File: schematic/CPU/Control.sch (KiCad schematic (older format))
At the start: 62 parts, among them U44 74LS273, U45 74LS273, U48 28C64, U49 28C64, U61 74LS08, U62 74LS86, U63 74LS374, U64 74LS00, U65 74LS32, U66 74LS08, U67 74LS08, U68 NA555P

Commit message: schematic finished
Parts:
- removed C4: 10nF, symbol Device:C_Small
- removed C5, C6: 0.1uF, symbol Device:C_Small
- removed D33: instrWE, LED_THT:LED_D3.0mm, symbol Device:LED
- removed D34: instrSel, LED_THT:LED_D3.0mm, symbol Device:LED
- removed D35: ~aluOE~, LED_THT:LED_D3.0mm, symbol Device:LED
- removed D36: aluYWE, LED_THT:LED_D3.0mm, symbol Device:LED
- removed D37: reg0WE, LED_THT:LED_D3.0mm, symbol Device:LED
- removed D38: reg1WE, LED_THT:LED_D3.0mm, symbol Device:LED
- removed D39: regBusSel, LED_THT:LED_D3.0mm, symbol Device:LED
- removed D40: ~regBusOE~, LED_THT:LED_D3.0mm, symbol Device:LED
- removed D41: aluSel, LED_THT:LED_D3.0mm, symbol Device:LED
- removed D42: marWE, LED_THT:LED_D3.0mm, symbol Device:LED
- removed D43: ramWE, LED_THT:LED_D3.0mm, symbol Device:LED
- removed D44: ramOE, LED_THT:LED_D3.0mm, symbol Device:LED
- removed D45, D47, D50: LED, LED_THT:LED_D3.0mm, symbol Device:LED
- removed D46: ramSelect, LED_THT:LED_D3.0mm, symbol Device:LED
- removed D48: ~pcOE~, LED_THT:LED_D3.0mm, symbol Device:LED
- removed D49: ~inOE~, LED_THT:LED_D3.0mm, symbol Device:LED
- removed D51: pcIncr, LED_THT:LED_D3.0mm, symbol Device:LED
- removed R33, R34, R35, R36, R37, R38, R39, R40, R41, R42, R43, R44, R45, R46, R47, R48, R49, R50, R51, R54, R58: 1k, Resistor_THT:R_Axial_DIN0207_L6.3mm_D2.5mm_P7.62mm_Horizontal, symbol Device:R
- removed R55: 10k, Resistor_THT:R_Axial_DIN0207_L6.3mm_D2.5mm_P7.62mm_Horizontal, symbol Device:R
- removed U68: NA555P, Package_DIP:DIP-8_W7.62mm, symbol Timer:NA555P
- added D? (x8): LED, LED_THT:LED_D3.0mm, symbol Device:LED
- added R? (x8): 1k, Resistor_THT:R_Axial_DIN0207_L6.3mm_D2.5mm_P7.62mm_Horizontal, symbol Device:R
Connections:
- net labels added: ca0, ca1, ca2, ca3, ca4, ca5, ca6, ca7, halt
- net labels removed: haltPulse
- wire segments 140 -> 114
- no-connect marks 29 -> 28
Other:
- moved on the sheet: R59, R60, R61, U44, U45, U61A, U61B, U61C, U61D, U61E, U62A, U62B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

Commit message: pre upgrade to vivado 2021
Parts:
- gave numbers to parts that had none: 16
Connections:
- net labels added: ~ctrlReg0WE~, ~ctrlReg1WE~
- net labels removed: ctrlReg0WE, ctrlReg1WE
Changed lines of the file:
@@
 $Descr A3 16535 11693
 encoding utf-8
-Sheet 16 19
+Sheet 15 20
 Title ""
 Date ""
@@
 ctrlAluSub
 Text GLabel 8350 5350 2    50   Output ~ 0
-ctrlReg0WE
+~ctrlReg0WE~
 Text GLabel 8350 5450 2    50   Output ~ 0
-ctrlReg1WE
+~ctrlReg1WE~
 Text GLabel 8350 5750 2    50   Output ~ 0
 ctrlAluSel
@@
 AR Path="/601B5CAE/622ED502" Ref="R?"  Part="1"
 AR Path="/6015C763/622ED502" Ref="R?"  Part="1"
-AR Path="/601BB1C4/622ED502" Ref="R?"  Part="1"
-F 0 "R?" V 9443 7750 50  0000 C CNN
+AR Path="/601BB1C4/622ED502" Ref="R43"  Part="1"
+F 0 "R43" V 9443 7750 50  0000 C CNN
 F 1 "1k" V 9534 7750 50  0000 C CNN
 F 2 "Resistor_THT:R_Axial_DIN0207_L6.3mm_D2.5mm_P7.62mm_Horizontal" V 9580 7750 50  0001 C CNN
@@
 AR Path="/601B5CAE/622ED508" Ref="D?"  Part="1"
 AR Path="/6015C763/622ED508" Ref="D?"  Part="1"
-AR Path="/601BB1C4/622ED508" Ref="D?"  Part="1"
-F 0 "D?" H 9993 7495 50  0000 C CNN
+AR Path="/601BB1C4/622ED508" Ref="D33"  Part="1"
+F 0 "D33" H 9993 7495 50  0000 C CNN
 F 1 "LED" H 9993 7586 50  0000 C CNN
 F 2 "LED_THT:LED_D3.0mm" H 10000 7750 50  0001 C CNN
@@
 AR Path="/601B5CAE/622ED518" Ref="R?"  Part="1"
 AR Path="/6015C763/622ED518" Ref="R?"  Part="1"
-AR Path="/601BB1C4/622ED518" Ref="R?"  Part="1"
-F 0 "R?" V 9443 8100 50  0000 C CNN
+AR Path="/601BB1C4/622ED518" Ref="R44"  Part="1"
+F 0 "R44" V 9443 8100 50  0000 C CNN
 F 1 "1k" V 9534 8100 50  0000 C CNN
 F 2 "Resistor_THT:R_Axial_DIN0207_L6.3mm_D2.5mm_P7.62mm_Horizontal" V 9580 8100 50  0001 C CNN
@@
 AR Path="/601B5CAE/622ED51E" Ref="D?"  Part="1"
 AR Path="/6015C763/622ED51E" Ref="D?"  Part="1"
-AR Path="/601BB1C4/622ED51E" Ref="D?"  Part="1"
-F 0 "D?" H 9993 7845 50  0000 C CNN
+AR Path="/601BB1C4/622ED51E" Ref="D34"  Part="1"
+F 0 "D34" H 9993 7845 50  0000 C CNN
 F 1 "LED" H 9993 7936 50  0000 C CNN
 F 2 "LED_THT:LED_D3.0mm" H 10000 8100 50  0001 C CNN
@@
 AR Path="/601B5CAE/622ED525" Ref="#PWR?"  Part="1"
 AR Path="/6015C763/622ED525" Ref="#PWR?"  Part="1"
-AR Path="/601BB1C4/622ED525" Ref="#PWR?"  Part="1"
-F 0 "#PWR?" H 10150 7850 50  0001 C CNN
+AR Path="/601BB1C4/622ED525" Ref="#PWR0180"  Part="1"
+F 0 "#PWR0180" H 10150 7850 50  0001 C CNN
 F 1 "GND" H 10155 7927 50  0000 C CNN
 F 2 "" H 10150 8100 50  0001 C CNN
@@
 AR Path="/601B5CAE/622ED52B" Ref="R?"  Part="1"
 AR Path="/6015C763/622ED52B" Ref="R?"  Part="1"
-AR Path="/601BB1C4/622ED52B" Ref="R?"  Part="1"
-F 0 "R?" V 9443 8450 50  0000 C CNN
+AR Path="/601BB1C4/622ED52B" Ref="R45"  Part="1"
+F 0 "R45" V 9443 8450 50  0000 C CNN
 F 1 "1k" V 9534 8450 50  0000 C CNN
 F 2 "Resistor_THT:R_Axial_DIN0207_L6.3mm_D2.5mm_P7.62mm_Horizontal" V 9580 8450 50  0001 C CNN
@@
 AR Path="/601B5CAE/622ED531" Ref="D?"  Part="1"
 AR Path="/6015C763/622ED531" Ref="D?"  Part="1"
-AR Path="/601BB1C4/622ED531" Ref="D?"  Part="1"
-F 0 "D?" H 9993 8195 50  0000 C CNN
+AR Path="/601BB1C4/622ED531" Ref="D35"  Part="1"
+F 0 "D35" H 9993 8195 50  0000 C CNN
 F 1 "LED" H 9993 8286 50  0000 C CNN
 F 2 "LED_THT:LED_D3.0mm" H 10000 8450 50  0001 C CNN
@@
 AR Path="/601B5CAE/622ED538" Ref="#PWR?"  Part="1"
 AR Path="/6015C763/622ED538" Ref="#PWR?"  Part="1"
-AR Path="/601BB1C4/622ED538" Ref="#PWR?"  Part="1"
-F 0 "#PWR?" H 10150 8200 50  0001 C CNN
+AR Path="/601BB1C4/622ED538" Ref="#PWR0181"  Part="1"
+F 0 "#PWR0181" H 10150 8200 50  0001 C CNN
 F 1 "GND" H 10155 8277 50  0000 C CNN
 F 2 "" H 10150 8450 50  0001 C CNN
@@
 AR Path="/601B5CAE/622ED53E" Ref="R?"  Part="1"
 AR Path="/6015C763/622ED53E" Ref="R?"  Part="1"
-AR Path="/601BB1C4/622ED53E" Ref="R?"  Part="1"
-F 0 "R?" V 9443 8800 50  0000 C CNN
+AR Path="/601BB1C4/622ED53E" Ref="R46"  Part="1"
+F 0 "R46" V 9443 8800 50  0000 C CNN
 F 1 "1k" V 9534 8800 50  0000 C CNN
 F 2 "Resistor_THT:R_Axial_DIN0207_L6.3mm_D2.5mm_P7.62mm_Horizontal" V 9580 8800 50  0001 C CNN
@@
 AR Path="/601B5CAE/622ED544" Ref="D?"  Part="1"
 AR Path="/6015C763/622ED544" Ref="D?"  Part="1"
-AR Path="/601BB1C4/622ED544" Ref="D?"  Part="1"
-F 0 "D?" H 9993 8545 50  0000 C CNN
+AR Path="/601BB1C4/622ED544" Ref="D36"  Part="1"
+F 0 "D36" H 9993 8545 50  0000 C CNN
 F 1 "LED" H 9993 8636 50  0000 C CNN
 F 2 "LED_THT:LED_D3.0mm" H 10000 8800 50  0001 C CNN
@@
 AR Path="/601B5CAE/622ED54B" Ref="#PWR?"  Part="1"
 AR Path="/6015C763/622ED54B" Ref="#PWR?"  Part="1"
-AR Path="/601BB1C4/622ED54B" Ref="#PWR?"  Part="1"
-F 0 "#PWR?" H 10150 8550 50  0001 C CNN
+AR Path="/601BB1C4/622ED54B" Ref="#PWR0182"  Part="1"
+F 0 "#PWR0182" H 10150 8550 50  0001 C CNN
 F 1 "GND" H 10155 8627 50  0000 C CNN
 F 2 "" H 10150 8800 50  0001 C CNN
@@
 AR Path="/601B5CAE/622ED552" Ref="R?"  Part="1"
 AR Path="/6015C763/622ED552" Ref="R?"  Part="1"
-AR Path="/601BB1C4/622ED552" Ref="R?"  Part="1"
-F 0 "R?" V 9443 9150 50  0000 C CNN
+AR Path="/601BB1C4/622ED552" Ref="R47"  Part="1"
+F 0 "R47" V 9443 9150 50  0000 C CNN
 F 1 "1k" V 9534 9150 50  0000 C CNN
 F 2 "Resistor_THT:R_Axial_DIN0207_L6.3mm_D2.5mm_P7.62mm_Horizontal" V 9580 9150 50  0001 C CNN
@@
 AR Path="/601B5CAE/622ED558" Ref="D?"  Part="1"
 AR Path="/6015C763/622ED558" Ref="D?"  Part="1"
-AR Path="/601BB1C4/622ED558" Ref="D?"  Part="1"
-F 0 "D?" H 9993 8895 50  0000 C CNN
+AR Path="/601BB1C4/622ED558" Ref="D37"  Part="1"
+F 0 "D37" H 9993 8895 50  0000 C CNN
 F 1 "LED" H 9993 8986 50  0000 C CNN
 F 2 "LED_THT:LED_D3.0mm" H 10000 9150 50  0001 C CNN
@@
 AR Path="/601B5CAE/622ED55F" Ref="#PWR?"  Part="1"
 AR Path="/6015C763/622ED55F" Ref="#PWR?"  Part="1"
-AR Path="/601BB1C4/622ED55F" Ref="#PWR?"  Part="1"
-F 0 "#PWR?" H 10150 8900 50  0001 C CNN
+AR Path="/601BB1C4/622ED55F" Ref="#PWR0183"  Part="1"
+F 0 "#PWR0183" H 10150 8900 50  0001 C CNN
 F 1 "GND" H 10155 8977 50  0000 C CNN
 F 2 "" H 10150 9150 50  0001 C CNN
@@
 AR Path="/601B5CAE/622ED566" Ref="R?"  Part="1"
 AR Path="/6015C763/622ED566" Ref="R?"  Part="1"
-AR Path="/601BB1C4/622ED566" Ref="R?"  Part="1"
-F 0 "R?" V 9443 9500 50  0000 C CNN
+AR Path="/601BB1C4/622ED566" Ref="R48"  Part="1"
+F 0 "R48" V 9443 9500 50  0000 C CNN
 F 1 "1k" V 9534 9500 50  0000 C CNN
 F 2 "Resistor_THT:R_Axial_DIN0207_L6.3mm_D2.5mm_P7.62mm_Horizontal" V 9580 9500 50  0001 C CNN
@@
 AR Path="/601B5CAE/622ED56C" Ref="D?"  Part="1"
 AR Path="/6015C763/622ED56C" Ref="D?"  Part="1"
-AR Path="/601BB1C4/622ED56C" Ref="D?"  Part="1"
-F 0 "D?" H 9993 9245 50  0000 C CNN
+AR Path="/601BB1C4/622ED56C" Ref="D38"  Part="1"
+F 0 "D38" H 9993 9245 50  0000 C CNN
 F 1 "LED" H 9993 9336 50  0000 C CNN
 F 2 "LED_THT:LED_D3.0mm" H 10000 9500 50  0001 C CNN
@@
 AR Path="/601B5CAE/622ED573" Ref="#PWR?"  Part="1"
 AR Path="/6015C763/622ED573" Ref="#PWR?"  Part="1"
-AR Path="/601BB1C4/622ED573" Ref="#PWR?"  Part="1"
-F 0 "#PWR?" H 10150 9250 50  0001 C CNN
+AR Path="/601BB1C4/622ED573" Ref="#PWR0184"  Part="1"
+F 0 "#PWR0184" H 10150 9250 50  0001 C CNN
 F 1 "GND" H 10155 9327 50  0000 C CNN
 F 2 "" H 10150 9500 50  0001 C CNN
@@
 AR Path="/601B5CAE/622ED57A" Ref="R?"  Part="1"
 AR Path="/6015C763/622ED57A" Ref="R?"  Part="1"
-AR Path="/601BB1C4/622ED57A" Ref="R?"  Part="1"
-F 0 "R?" V 9443 9850 50  0000 C CNN
+AR Path="/601BB1C4/622ED57A" Ref="R49"  Part="1"
+F 0 "R49" V 9443 9850 50  0000 C CNN
 F 1 "1k" V 9534 9850 50  0000 C CNN
 F 2 "Resistor_THT:R_Axial_DIN0207_L6.3mm_D2.5mm_P7.62mm_Horizontal" V 9580 9850 50  0001 C CNN
@@
 AR Path="/601B5CAE/622ED580" Ref="D?"  Part="1"
 AR Path="/6015C763/622ED580" Ref="D?"  Part="1"
-AR Path="/601BB1C4/622ED580" Ref="D?"  Part="1"
-F 0 "D?" H 9993 9595 50  0000 C CNN
+AR Path="/601BB1C4/622ED580" Ref="D39"  Part="1"
+F 0 "D39" H 9993 9595 50  0000 C CNN
 F 1 "LED" H 9993 9686 50  0000 C CNN
 F 2 "LED_THT:LED_D3.0mm" H 10000 9850 50  0001 C CNN
@@
 AR Path="/601B5CAE/622ED587" Ref="#PWR?"  Part="1"
 AR Path="/6015C763/622ED587" Ref="#PWR?"  Part="1"
-AR Path="/601BB1C4/622ED587" Ref="#PWR?"  Part="1"
-F 0 "#PWR?" H 10150 9600 50  0001 C CNN
+AR Path="/601BB1C4/622ED587" Ref="#PWR0185"  Part="1"
+F 0 "#PWR0185" H 10150 9600 50  0001 C CNN
 F 1 "GND" H 10155 9677 50  0000 C CNN
 F 2 "" H 10150 9850 50  0001 C CNN
@@
 AR Path="/601B5CAE/622ED58E" Ref="R?"  Part="1"
 AR Path="/6015C763/622ED58E" Ref="R?"  Part="1"
-AR Path="/601BB1C4/622ED58E" Ref="R?"  Part="1"
-F 0 "R?" V 9443 10200 50  0000 C CNN
+AR Path="/601BB1C4/622ED58E" Ref="R50"  Part="1"
+F 0 "R50" V 9443 10200 50  0000 C CNN
 F 1 "1k" V 9534 10200 50  0000 C CNN
 F 2 "Resistor_THT:R_Axial_DIN0207_L6.3mm_D2.5mm_P7.62mm_Horizontal" V 9580 10200 50  0001 C CNN
@@
 AR Path="/601B5CAE/622ED594" Ref="D?"  Part="1"
 AR Path="/6015C763/622ED594" Ref="D?"  Part="1"
-AR Path="/601BB1C4/622ED594" Ref="D?"  Part="1"
-F 0 "D?" H 9993 9945 50  0000 C CNN
+AR Path="/601BB1C4/622ED594" Ref="D40"  Part="1"
+F 0 "D40" H 9993 9945 50  0000 C CNN
 F 1 "LED" H 9993 10036 50  0000 C CNN
 F 2 "LED_THT:LED_D3.0mm" H 10000 10200 50  0001 C CNN
@@
 AR Path="/601B5CAE/622ED59B" Ref="#PWR?"  Part="1"
 AR Path="/6015C763/622ED59B" Ref="#PWR?"  Part="1"
-AR Path="/601BB1C4/622ED59B" Ref="#PWR?"  Part="1"
-F 0 "#PWR?" H 10150 9950 50  0001 C CNN
+AR Path="/601BB1C4/622ED59B" Ref="#PWR0186"  Part="1"
+F 0 "#PWR0186" H 10150 9950 50  0001 C CNN
 F 1 "GND" H 10155 10027 50  0000 C CNN
 F 2 "" H 10150 10200 50  0001 C CNN
@@
 AR Path="/601B5CAE/622ED5A4" Ref="#PWR?"  Part="1"
 AR Path="/6015C763/622ED5A4" Ref="#PWR?"  Part="1"
-AR Path="/601BB1C4/622ED5A4" Ref="#PWR?"  Part="1"
-F 0 "#PWR?" H 10150 7500 50  0001 C CNN
+AR Path="/601BB1C4/622ED5A4" Ref="#PWR0179"  Part="1"
+F 0 "#PWR0179" H 10150 7500 50  0001 C CNN
 F 1 "GND" H 10155 7577 50  0000 C CNN
 F 2 "" H 10150 7750 50  0001 C CNN

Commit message: fibonacci works again with new memory design
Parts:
- removed U45: 74LS273, Package_DIP:DIP-20_W7.62mm, symbol 74xx:74LS273
- removed unit 4 of U64
- removed unit 4 of U66
- added U53: 74AS825, symbol 74xx:74AS825
- added U54: 28C64, Package_DIP:DIP-28_W15.24mm, symbol Memory_EEPROM:28C64
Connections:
- net labels added: ctrlMemInstrImmToRam, ctrlMemSPUp, ctrlRegAluSel, instrCode0, instrCode1, instrCode2, instrCode3, instrCode4, instrCode5, instrCode6, instrCode7, ~ctrlAluYWE~, ~ctrlInstrWE~, ~ctrlMemInstrOE~, ~ctrlMemInstrWE~, ~ctrlMemMar0WE~, ~ctrlMemMar1WE~, ~ctrlMemPCIncr~, ~ctrlMemPCLoad~, ~ctrlMemRamOE~, ~ctrlMemRamWE~, ~ctrlMemSPEn~
- net labels removed: b0, b1, b2, b3, b4, b5, b6, b7, ctrlAluSel, ctrlAluYWE, ctrlInstrPulse, ctrlInstrSel, ctrlMarWE, ctrlPCIncr, ctrlPCLoad, ctrlRamOE, ctrlRamSelect, ctrlRamWE, outWE, ~ctrlPCOE~, ~inOE~
- wire segments 114 -> 126
- no-connect marks 28 -> 35
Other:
- note added: "(step==1) := ~(!a0 + a1 + a2)~"
- note added: "micro0"
- note added: "micro1"
- note added: "micro2"
- note removed: "instrEqual1 = ~(!a0 + a1 + a2)~"
- moved on the sheet: R43, R44, R45, R46, R47, R48, R49, R50, U66A, U66B, U66C, U67A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

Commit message: schematic with henry
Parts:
- removed D33, D34, D35, D36, D37, D38, D39, D40: LED, LED_THT:LED_D3.0mm, symbol Device:LED
- removed D52: step0, LED_THT:LED_D3.0mm, symbol Device:LED
- removed D53: step1, LED_THT:LED_D3.0mm, symbol Device:LED
- removed D54: step2, LED_THT:LED_D3.0mm, symbol Device:LED
- removed R43, R44, R45, R46, R47, R48, R49, R50, R59, R60, R61: 1k, Resistor_THT:R_Axial_DIN0207_L6.3mm_D2.5mm_P7.62mm_Horizontal, symbol Device:R
- removed U44: 74LS273, Package_DIP:DIP-20_W7.62mm, symbol 74xx:74LS273
- removed U48, U49, U54: 28C64, Package_DIP:DIP-28_W15.24mm, symbol Memory_EEPROM:28C64
- removed U53: 74AS825, symbol 74xx:74AS825
- removed U64: 74LS00, Package_DIP:DIP-14_W7.62mm, symbol 74xx:74LS00
- removed U65: 74LS32, Package_DIP:DIP-14_W7.62mm, symbol 74xx:74LS32
- removed U66, U67: 74LS08, symbol 74xx:74LS08
- added D49, D50, D51, D52, D53, D54, D55, D56: LED_Small, symbol Device:LED_Small
- added RN11: 220, Resistor_THT:R_Array_SIP9, symbol Device:R_Network08
- added U83: 74AS825, symbol 8bitCPU-rescue:74AS825-74xx
- added U85, U86, U87: 28C256, symbol Memory_EEPROM:28C256
- added U96: 74ABT540, symbol 8bitCPU-rescue:74ABT540
- renumbered U61 to U38, U61 to U59, U61 to U78, U62 to U81, U61 to U82, U63 to U84
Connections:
- net labels added: a13, a14, flagCarry, flagOverflow, ~ctrlInstrFinished~, ~ctrlMemPC0FromBus~, ~ctrlMemPC1FromBus~, ~ctrlMemPCEn~, ~ctrlReg0BusOE~, ~ctrlReg1BusOE~
- net labels removed: ca0, ca1, ca2, ca3, ca4, ca5, ca6, ca7, clk, ctrlRegBusSel, ~ctrlInstrWE~, ~ctrlMemPCIncr~, ~ctrlRegBusOE~
- wire segments 126 -> 93
- no-connect marks 35 -> 14
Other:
- note added: "0-3: flags\n5-7: stepReg"
- note removed: "(step==1) := ~(!a0 + a1 + a2)~"
- note removed: "3-4: flags\n5-7: stepReg"
- note removed: "instruction and reduction for halt"
- moved on the sheet: U38B, U59C, U78A, U81A, U81E, U82E

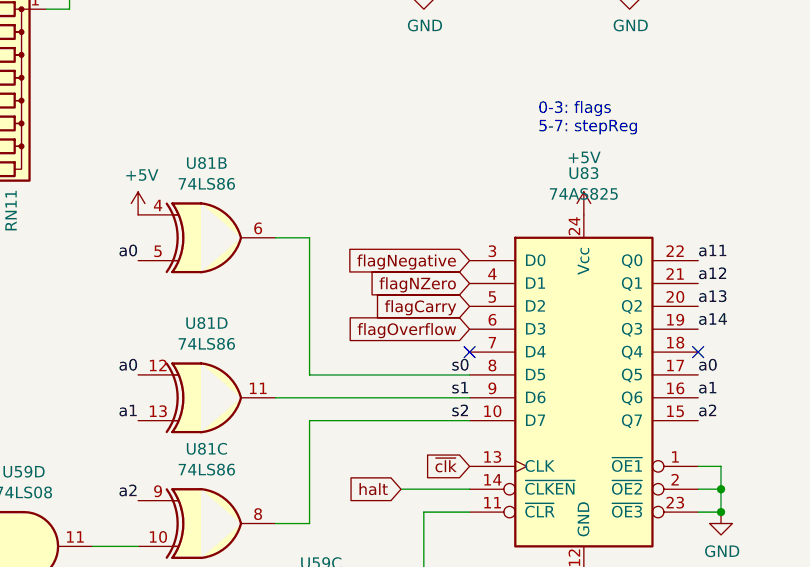
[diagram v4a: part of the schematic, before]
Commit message: updated some more verilog
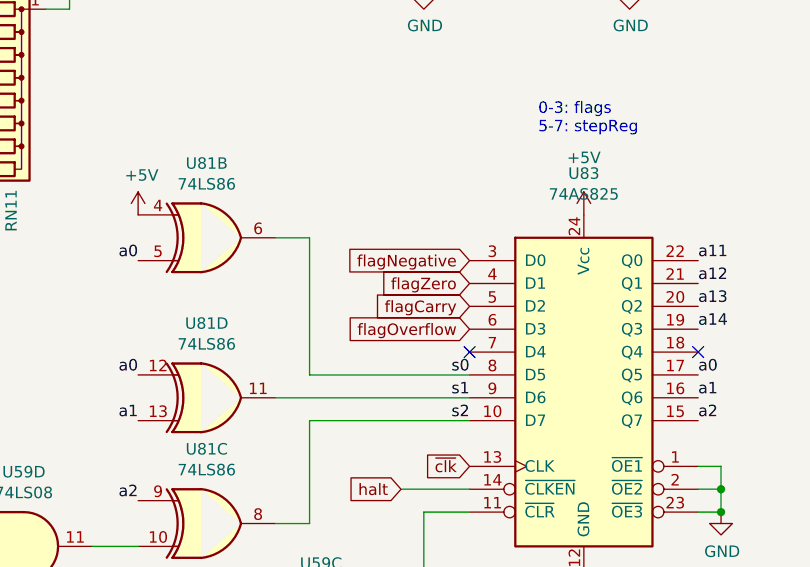
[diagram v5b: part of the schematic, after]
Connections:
- net flagNZero renamed flagZero
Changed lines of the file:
@@
 instrCode6
 Text GLabel 5250 5400 0    50   Input ~ 0
-flagNZero
+flagZero
 Text GLabel 5250 5300 0    50   Input ~ 0
 flagNegative

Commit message: renamed project
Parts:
- U83: symbol 8bitCPU-rescue:74AS825-74xx -> MEDiC-rescue:74AS825-74xx
- U96: symbol 8bitCPU-rescue:74ABT540 -> MEDiC-rescue:74ABT540
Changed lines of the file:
@@
 ~ctrlMemPC1FromBus~
 $Comp
-L 8bitCPU-rescue:74AS825-74xx U?
+L MEDiC-rescue:74AS825-74xx U?
 U 1 1 6152118F
 P 5750 5800
@@
 ~ctrlInstrFinished~
 $Comp
-L 8bitCPU-rescue:74ABT540 U?
+L MEDiC-rescue:74ABT540 U?
 U 1 1 63C4D029
 P 2000 4700

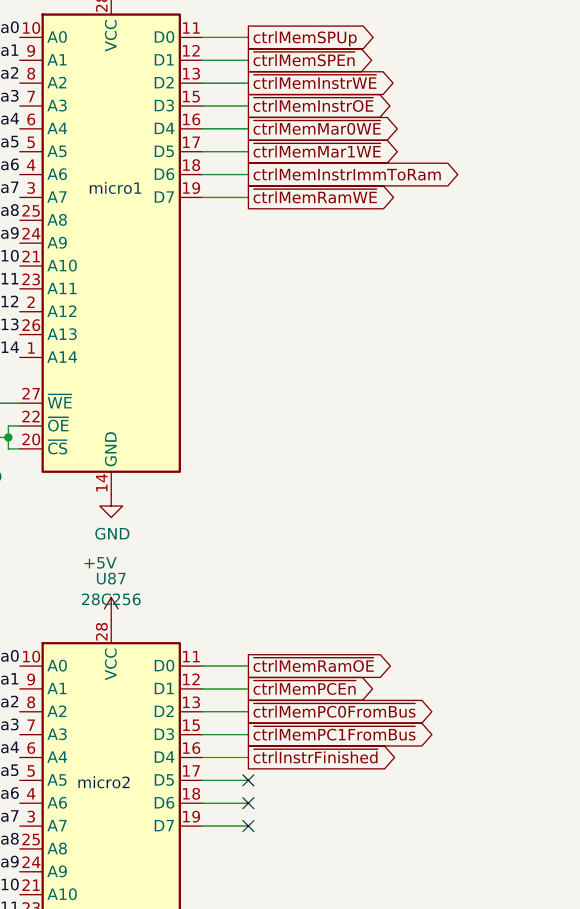
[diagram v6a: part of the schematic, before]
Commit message: fibonacci works again, sp etc needs to be tested
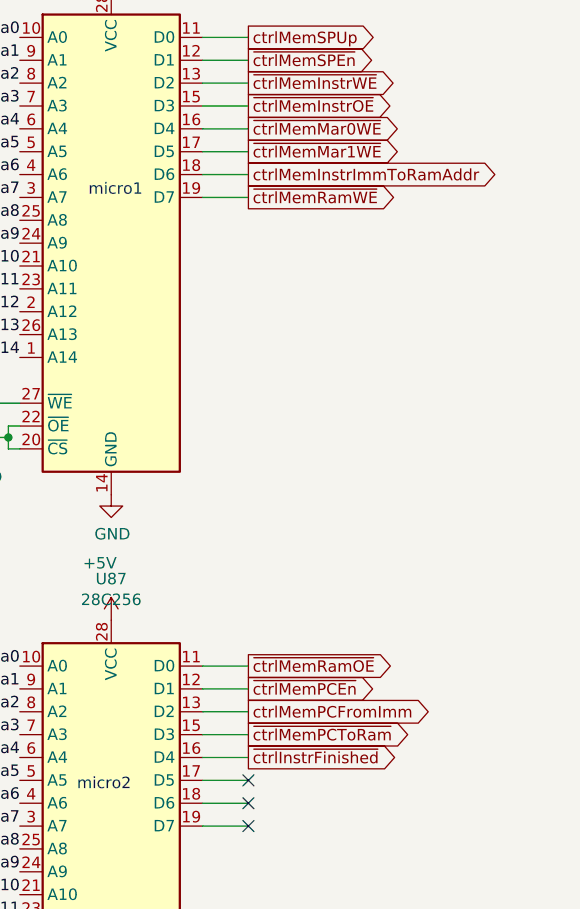
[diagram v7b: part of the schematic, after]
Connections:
- net ctrlMemInstrImmToRam renamed ctrlMemInstrImmToRamAddr
- net ~ctrlMemPC0FromBus~ renamed ctrlMemPCFromImm
- net ~ctrlMemPC1FromBus~ renamed ~ctrlMemPCToRam~
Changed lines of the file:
@@
 $EndComp
 Text GLabel 9750 6750 2    50   Output ~ 0
-ctrlMemInstrImmToRam
+ctrlMemInstrImmToRamAddr
 Text GLabel 9750 6550 2    50   Output ~ 0
 ~ctrlMemMar0WE~
@@
 Text GLabel 9750 6850 2    50   Output ~ 0
 ~ctrlMemRamWE~
-NoConn ~ 9750 9400
 NoConn ~ 9750 9500
 Text GLabel 9750 8900 2    50   Output ~ 0
@@
 Wire Wire Line
 	9550 9000 9750 9000
-Text GLabel 9750 9100 2    50   Output ~ 0
-~ctrlMemPC0FromBus~
-Text GLabel 9750 9200 2    50   Output ~ 0
-~ctrlMemPC1FromBus~
 $Comp
 L MEDiC-rescue:74AS825-74xx U?
@@
 Wire Wire Line
 	1100 4900 1100 4800
+Text GLabel 9750 9200 2    50   Output ~ 0
+~ctrlMemPCToRam~
+Text GLabel 9750 9100 2    50   Output ~ 0
+ctrlMemPCFromImm
+NoConn ~ 9750 9400
 $EndSCHEMATC

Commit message: renamed project
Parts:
- U83: symbol MEDiC-rescue:74AS825-74xx -> EDiC-rescue:74AS825-74xx
- U96: symbol MEDiC-rescue:74ABT540 -> EDiC-rescue:74ABT540
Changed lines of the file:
@@
 	9550 9000 9750 9000
 $Comp
-L MEDiC-rescue:74AS825-74xx U?
+L EDiC-rescue:74AS825-74xx U?
 U 1 1 6152118F
 P 5750 5800
@@
 ~ctrlInstrFinished~
 $Comp
-L MEDiC-rescue:74ABT540 U?
+L EDiC-rescue:74ABT540 U?
 U 1 1 63C4D029
 P 2000 4700
